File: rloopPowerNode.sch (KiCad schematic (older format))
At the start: 13 parts

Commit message: Switch to DPDT relay and rearranged stuff
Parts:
- removed K? (x2): RELAY, symbol RELAY
- removed Q?: Q_NJFET_DGS, symbol Q_NJFET_DGS
- removed U?: 74LS32, symbol 74LS32
- removed U?: Regulator, symbol Regulator
- removed U?: IsolatedRegulator, symbol IsolatedRegulator
- added C? (x2): C, symbol C
- added Q? (x2): Q_NMOS_GSD, symbol Q_NMOS_GSD
- added R? (x3): R, symbol R
- added RL?: Relay_DPDT, symbol Relay_DPDT
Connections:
- net labels added: DCDC_Vin+, DCDC_Vin-, LVEnablePin
- net labels removed: NodeControlPin
- wire segments 23 -> 33
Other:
- moved on the sheet: 10k, D?, R?, SW?

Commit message: work began
laid out some of the top level

started some lower level sub-circuits, such as relay drivers
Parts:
- removed 10k, R? (x5): R, symbol R
- removed C? (x2): C, symbol C
- removed D?: D, symbol D
- removed D?: LED, symbol LED
- removed Q? (x2): Q_NMOS_GSD, symbol Q_NMOS_GSD
- removed RL?: Relay_DPDT, symbol Relay_DPDT
- removed SW?: Switch_3PST, symbol Switch_3PST
- removed U?: 4541, symbol 4541
- added A?: Teensy_3.2, symbol Teensy_3.2
- added A?: RASPI_2B, symbol RASPI_2B
- added P?: CONN_01X09, symbol CONN_01X09
- added R? (x2): R, symbol R
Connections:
- net labels added: GLV, GNDA, HV-CURR, OSBMS-CLK, OSBMS-CS, OSBMS-IRQ, OSBMS-MISO, OSBMS-MOSI, OSBMS-PDLOWOUT, OSBMS-SCK, Pi-SCL, Pi-SDA, RLY-24V-HIGH, RLY-24V-LOW, RLY-ISO-HIGH, RLY-ISO-LOW, SENS-SCL, SENS-SDA
- net labels removed: +5V, +BATT, -BATT, DCDC_Vin+, DCDC_Vin-, LVEnablePin
- wire segments 33 -> 87
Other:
- note added: "To ATA6870\nOpen Source BMS"

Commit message: added some ICs, started on power, changed sheet sizes
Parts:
- added C? (x5): 100n, symbol C
- added P? (x4): CONN_01X02, symbol CONN_01X02
- added P?: CONN_01X04, Pin_Headers:Pin_Header_Straight_1x04_Pitch2.00mm, symbol CONN_01X04
- added U?: MCP2562, symbol MCP2562
- added U?: TYS01, symbol TYS01
- added U?: ISO1540, symbol ISO1540
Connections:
- net labels added: +3.3V, CAN-RX, CAN-TX
- wire segments 87 -> 162
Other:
- note added: "To baro sensor"

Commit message: near done, TODO needs 5V sup from HV, etc
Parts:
- removed A?: Teensy_3.2, symbol Teensy_3.2
- removed A?: RASPI_2B, symbol RASPI_2B
- removed C? (x4): 100n, symbol C
- removed P?: CONN_01X04, Pin_Headers:Pin_Header_Straight_1x04_Pitch2.00mm, symbol CONN_01X04
- removed R? (x2): R, symbol R
- removed U?: MCP2562, symbol MCP2562
- removed U?: TYS01, symbol TYS01
- removed U?: ISO1540, symbol ISO1540
- added A?: NODE_CORE_CONNECTOR, symbol NODE_CORE_CONNECTOR
- added C? (x3): 100n, symbol C
- added C? (x2): 1u, symbol C
- added D?: ZENER +2V8, symbol ZENER
- added P? (x4): CONN_01X03, Pin_Headers:Pin_Header_Angled_1x03, symbol CONN_01X03
- added P?: SHUNT, symbol CONN_01X02
- added Q?: BSS84, TO_SOT_Packages_SMD:SOT-23, symbol Q_PMOS_GSD
- added R?: 1M, Resistors_SMD:R_1206_HandSoldering, symbol R
- added R?: 100K, symbol R
- added R?: R, symbol R
- added U?: MS5607-02BA03, symbol MS5607-02BA03
- added U?: DS2482-100, symbol DS2482-100
- added U?: AMC1100, symbol AMC1100
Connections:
- net labels added: +5V-HV, HV-GND
- net labels removed: CAN-RX, CAN-TX, Pi-SCL, Pi-SDA
- wire segments 162 -> 149
- no-connect marks 0 -> 2
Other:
- note added: "4x strands, 10x sensors each"
- note added: "To ATA6870\nOpen Source BMS\nMultiple BMS will be daisy chained"
- note added: "barometric pressure sensor\nfor detecting depressurization"
- note added: "checks the GLV (+24V)"
- note added: "one temperature sensor for each cell"
- note added: "reads current from the HV battery\nlow side current shunt\nwhich is galvanically isolated"
- note removed: "To ATA6870\nOpen Source BMS"
- note removed: "To baro sensor"
- moved on the sheet: C?, P?

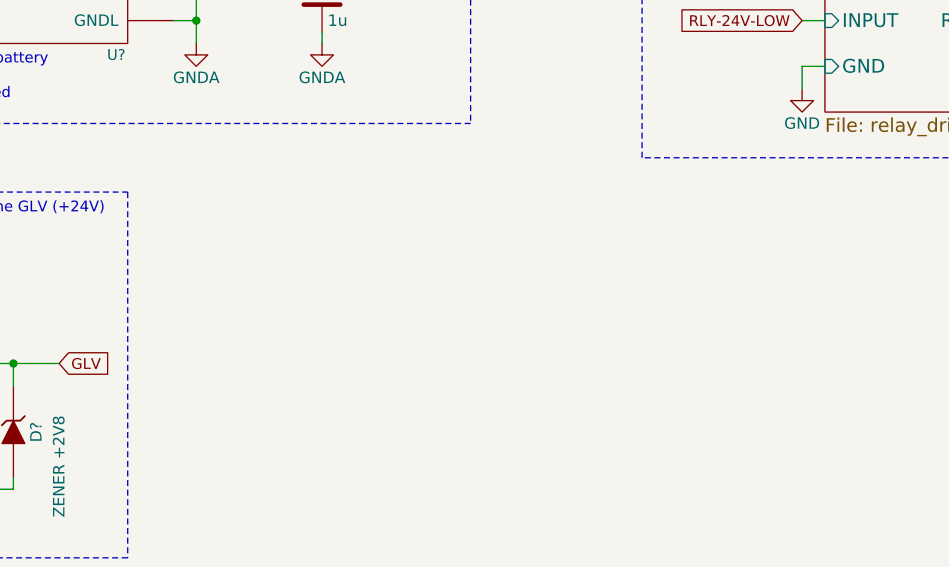
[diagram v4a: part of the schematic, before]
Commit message: added a 78L05 for the AMC1100
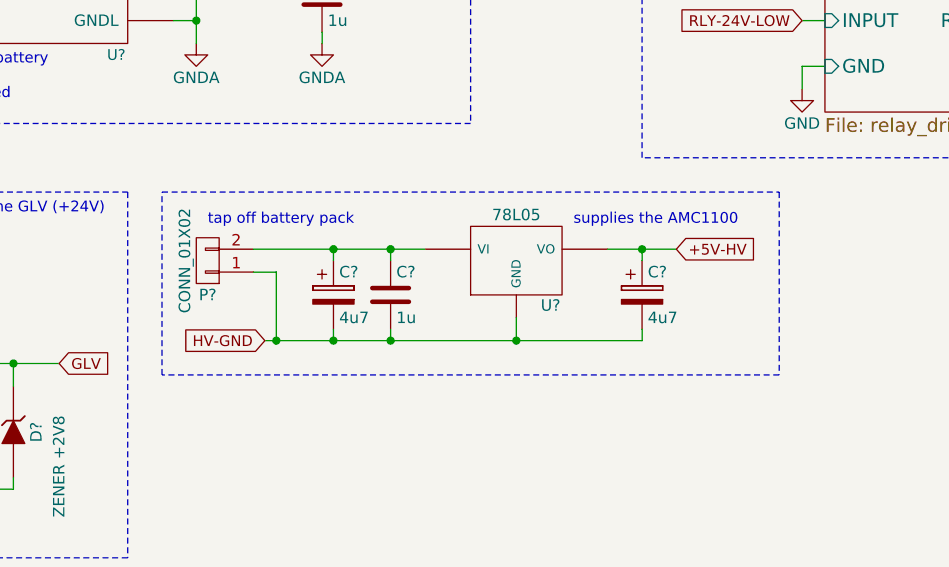
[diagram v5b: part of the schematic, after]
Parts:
- added C? (x2): 4u7, symbol CP
- added C?: 1u, symbol C
- added P?: CONN_01X02, symbol CONN_01X02
- added U?: 78L05, symbol 78L05
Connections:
- net Relay Driver/RELAY-NEG is gone; now on net Relay Driver/RELAY-NEG: P?.2 (P2)
- net Relay Driver/RELAY-POS is gone; now on net Relay Driver/RELAY-POS: P?.1 (P1)
- net +5V-HV: now also C?.1, U?.VO
- net HV-GND: now also C?.2, C?.2, C?.2, P?.1 (P1), U?.GND
- net Relay Driver/RELAY-NEG: no longer P?.2 (P2)
- net Relay Driver/RELAY-POS: no longer P?.1 (P1)
- new net: C?.1, C?.1, P?.2 (P2), U?.VI
- new net Relay Driver/RELAY-NEG: P?.2 (P2)
- new net Relay Driver/RELAY-POS: P?.1 (P1)
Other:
- note added: "supplies the AMC1100"
- note added: "tap off battery pack"
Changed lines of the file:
@@
 Wire Notes Line
 	8500 5250 8500 650
+$Comp
+L 78L05 U?
+U 1 1 573D5D57
+P 7950 5700
+F 0 "U?" H 8100 5504 50  0000 C CNN
+F 1 "78L05" H 7950 5900 50  0000 C CNN
+F 2 "" H 7950 5700 50  0000 C CNN
+F 3 "" H 7950 5700 50  0000 C CNN
+	1    7950 5700
+	1    0    0    -1
+$EndComp
+Text GLabel 6850 6050 0    47   Input ~ 0
+HV-GND
+$Comp
+L CONN_01X02 P?
+U 1 1 573D68FA
+P 6600 5700
+F 0 "P?" H 6600 5850 50  0000 C CNN
+F 1 "CONN_01X02" V 6700 5700 50  0000 C CNN
+F 2 "" H 6600 5700 50  0000 C CNN
+F 3 "" H 6600 5700 50  0000 C CNN
+	1    6600 5700
+	-1   0    0    1
+$EndComp
+$Comp
+L CP C?
+U 1 1 573D6D0A
+P 7150 5850
+F 0 "C?" H 7175 5950 50  0000 L CNN
+F 1 "4u7" H 7175 5750 50  0000 L CNN
+F 2 "" H 7188 5700 50  0000 C CNN
+F 3 "" H 7150 5850 50  0000 C CNN
+	1    7150 5850
+	1    0    0    -1
+$EndComp
+$Comp
+L C C?
+U 1 1 573D757D
+P 7400 5850
+F 0 "C?" H 7425 5950 50  0000 L CNN
+F 1 "1u" H 7425 5750 50  0000 L CNN
+F 2 "" H 7438 5700 50  0000 C CNN
+F 3 "" H 7400 5850 50  0000 C CNN
+	1    7400 5850
+	1    0    0    -1
+$EndComp
+$Comp
+L CP C?
+U 1 1 573D7783
+P 8500 5850
+F 0 "C?" H 8525 5950 50  0000 L CNN
+F 1 "4u7" H 8525 5750 50  0000 L CNN
+F 2 "" H 8538 5700 50  0000 C CNN
+F 3 "" H 8500 5850 50  0000 C CNN
+	1    8500 5850
+	1    0    0    -1
+$EndComp
+Wire Wire Line
+	6800 5750 6900 5750
+Wire Wire Line
+	6900 5750 6900 6050
+Wire Wire Line
+	6850 6050 8500 6050
+Wire Wire Line
+	8500 6050 8500 6000
+Connection ~ 6900 6050
+Wire Wire Line
+	7400 6000 7400 6050
+Connection ~ 7400 6050
+Wire Wire Line
+	7150 6000 7150 6050
+Connection ~ 7150 6050
+Wire Wire Line
+	7950 5950 7950 6050
+Connection ~ 7950 6050
+Wire Wire Line
+	8350 5650 8650 5650
+Wire Wire Line
+	8500 5700 8500 5650
+Connection ~ 8500 5650
+Wire Wire Line
+	7550 5650 6800 5650
+Wire Wire Line
+	7150 5700 7150 5650
+Connection ~ 7150 5650
+Wire Wire Line
+	7400 5700 7400 5650
+Connection ~ 7400 5650
+Text GLabel 8650 5650 2    47   Input ~ 0
++5V-HV
+Text Notes 8200 5550 0    47   ~ 0
+supplies the AMC1100
+Wire Notes Line
+	6400 5400 9100 5400
+Wire Notes Line
+	9100 5400 9100 6200
+Wire Notes Line
+	9100 6200 6400 6200
+Wire Notes Line
+	6400 6200 6400 5400
+Text Notes 6600 5550 0    47   ~ 0
+tap off battery pack
 $EndSCHEMATC

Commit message: wip showing you the latching power btn
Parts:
- added JP? (x8): Jumper_NC_Small, symbol Jumper_NC_Small
- added P? (x4): CONN_01X02, symbol CONN_01X02
- added P?: CONN_02X05, symbol CONN_02X05
- added R? (x3): R, symbol R
- added RL? (x3): Relay_DPDT, symbol Relay_DPDT
- added SW?: Switch_3PST, symbol Switch_3PST
- added U? (x2): LTV-358T, MFSOP-6, symbol LTV-358T
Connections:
- net GND: now also JP?.1, JP?.1, JP?.1, JP?.1, JP?.1, JP?.1, JP?.1, JP?.1, P?.10 (P10), P?.2 (P2), P?.4 (P4), P?.6 (P6), P?.8 (P8), U?.3
- net OSBMS-CS: now also P?.7 (P7)
- net OSBMS-MISO: now also P?.1 (P1)
- net OSBMS-MOSI: now also P?.3 (P3)
- net OSBMS-SCK: now also P?.5 (P5)
- net Relay Driver/RELAY-NEG: now also RL?.2; no longer P?.2 (P2)
- net Relay Driver/RELAY-POS: now also RL?.1; no longer P?.1 (P1)
- new net: P?.1 (P1), RL?.4, SW?.1
- new net: RL?.5, SW?.2
- new net: P?.2 (P2), RL?.7, SW?.3
- new net: RL?.8, SW?.4
- new net: P?.1 (P1), RL?.8
- new net: P?.2 (P2), R?.2, RL?.5
- new net: A?.~ (T9/RX2), JP?.2 (x8)
- new net: R?.2, RL?.1 (x2)
- new net: RL?.2, U?.6 (x2)
- new net: P?.2 (P2), R?.1, R?.1, R?.1, RL?.4, RL?.4
- new net: P?.1 (P1), RL?.7, U?.4, U?.4
- new net Relay Driver/RELAY-NEG: P?.2 (P2)
- new net Relay Driver/RELAY-POS: P?.1 (P1)
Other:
- note added: "one temperature sensor for every 2 cells"
- note removed: "one temperature sensor for each cell"
- moved on the sheet: A?, C?, D?, P?, Q?, R?, U?

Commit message: WIP but mostly done, needs connector
latch switch changed to using photorelays
added watchdog to relays
added two unidirectional precharge subcircuits
moved ILV relay to onboard
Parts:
- removed P? (x6): CONN_01X02, symbol CONN_01X02
- removed R? (x3): R, symbol R
- removed RL? (x3): Relay_DPDT, symbol Relay_DPDT
- removed SW?: Switch_3PST, symbol Switch_3PST
- removed U? (x2): LTV-358T, MFSOP-6, symbol LTV-358T
- added C?: 100n, symbol C
- added D? (x3): D, symbol D
- added JP?: JUMPER, symbol JUMPER
- added P?: CONN_01X02, symbol CONN_01X02
- added Q?: NMOS, symbol Q_NMOS_GDSD
- added Q? (x2): PMOS, symbol Q_PMOS_GDSD
- added R? (x4): 470, symbol R
- added R? (x3): 100K, symbol R
- added R?: 10K, symbol R
- added R?: 100, symbol R
- added R?: 1K, symbol R
- added R?: 10, symbol R
- added RL? (x2): Relay_DPDT, symbol Relay_DPDT
- added U? (x4): CPC1718, symbol CPC1718
- added U?: MAX6814, symbol WDT-5PIN-ACTIVELOW
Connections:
- net HV-GND is gone; now on net BATT-NEG: C?.1, C?.2, C?.2, C?.2, P?.1 (P1), P?.1 (P1), U?.3 (VinN), U?.4 (GNDH), U?.GND
- net RLY-24V-HIGH is gone; now on net SENS-SDA: A?.~ (T9/RX2)
- net RLY-24V-LOW is gone; now on net SENS-SDA: A?.~ (T9/RX2)
- net +3V3: now also C?.1, U?.5 (VDD)
- net BATT-NEG: now also RL?.7, U?.2, U?.2, U?.2
- net BATT-POS: now also Q?.3 (S), R?.1, RL?.4, U?.1
- net GND: now also C?.2, Q?.3 (S), R?.2, U?.2 (GND), U?.3, U?.3
- net Relay Driver/RELAY-NEG: now also RL?.2; no longer P?.2 (P2)
- net Relay Driver/RELAY-POS: now also RL?.1; no longer P?.1 (P1)
- net BMS-PWR: now reaches P?.9 (P9)
- net ILV+: now reaches C?.1, C?.1, P?.2 (P2), U?.VI
- net ILV+: now also RL?.5
- new net: R?.1, U?.3
- new net: D?.1 (K), U?.4
- new net: P?.1 (P1), U?.3
- new net: R?.2, U?.4
- new net: D?.2 (A), P?.2 (P2)
- new net: Q?.1 (G), R?.1
- new net: JP?.2, Q?.2 (D), Q?.4 (D)
- new net: R?.1, R?.2, U?.1 (~OUTPUT)
- new net: Q?.1 (G), R?.1, R?.2 (x2)
- new net: D?.2 (A), Q?.2 (D), Q?.4 (D) (x2)
- new net: R?.2, U?.1 (x2)
- new net: R?.1, U?.4 (x2)
- new net: D?.1 (K), R?.1 (x2)
- new net BATT-ILV: Q?.3 (S), R?.1, RL?.4
- new net DCDC-NEG: RL?.8, U?.1
- new net DCDC-POS: RL?.5, U?.2
- new net IHV-EXTERNAL: R?.2
- new net IHV-PRECHG: R?.2
- new net ILV-EXTERNAL: R?.2
- new net ILV-PRECHG: R?.2
- new net RELAY-COMMON: JP?.1
- new net RLY-ILV: A?.~ (T9/RX2)
- new net Relay Driver/RELAY-NEG: P?.2 (P2)
- new net Relay Driver/RELAY-NEG: RL?.2
- new net Relay Driver/RELAY-POS: P?.1 (P1)
- new net Relay Driver/RELAY-POS: RL?.1
- new net WDT: U?.4 (INPUT)
- no-connect marks 2 -> 3
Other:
- note added: "Precharge IHV"
- note added: "Precharge ILV"
- note added: "TODO: Give connectors to external stuff\nTODO: Pin assignments for unassigned signals\nTODO: Review suggested change to BMS connector\n"
- note added: "Use external battery as "ignition""
- note added: "Watchdog to kill all power"
- note added: "manual disconnect"
- note added: "suggested connector to Open Source BMS\nribbon cable with grounds add noise immunity"
- note removed: "tap off battery pack"
- moved on the sheet: A?, C?, D?, JP?, P?, Q?, R?, U?

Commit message: added GND fault detect, conns, no pending TODOs
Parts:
- removed D?: D, symbol D
- removed JP?: JUMPER, symbol JUMPER
- removed P?: CONN_01X09, symbol CONN_01X09
- removed Q? (x2): PMOS, symbol Q_PMOS_GDSD
- removed R? (x2): 470, symbol R
- removed R?: 10K, symbol R
- removed R? (x2): 100K, symbol R
- removed R?: 100, symbol R
- removed R?: 1K, symbol R
- removed R?: 10, symbol R
- removed RL?: Relay_DPDT, symbol Relay_DPDT
- removed U?: CPC1718, symbol CPC1718
- added D? (x2): D, symbol D
- added D?: ZENER +3V6, symbol ZENER
- added D?: LED, symbol Led_Small
- added F? (x2): FUSE, symbol FUSE
- added JP?: JUMPER3, symbol JUMPER3
- added P? (x7): CONN_01X02, symbol CONN_01X02
- added P? (x6): CONN_01X01, symbol CONN_01X01
- added P?: CONN_01X08, symbol CONN_01X08
- added Q?: PMOS, symbol Q_PMOS_GSD
- added Q?: NMOS, symbol Q_NMOS_GDSD
- added R? (x2): 100, symbol R
- added R?: 470, symbol R
- added R?: 100K, symbol R
- added R?: 10K, symbol R
- added R?: 1K8, symbol R
- added R?: 330, symbol R
- added R?: 10, symbol R
- added U?: CPC1718, symbol CPC1718
- added U?: H11F1SM, MFSOP-6, symbol OPTOISO
- C?: value 1u -> 100n
- D?: value ZENER +2V8 -> ZENER +2V7
- P?: value CONN_02X05 -> AMPMODU-02X05
- R?: value 1M -> 100K
- R?: value 100K -> 10K
- R?: value R -> 100
- R?: value 470 -> 100
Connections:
- net +24V: now also P?.2 (P2), P?.2 (P2)
- net +3V3: no longer C?.1, U?.5 (VDD)
- net BATT-ILV: now also P?.1 (P1), R?.2
- net BATT-NEG: now also P?.1 (P1); no longer C?.1, C?.2, C?.2, C?.2, P?.1 (P1), P?.1 (P1), U?.2, U?.3 (VinN), U?.4 (GNDH), U?.GND
- net BATT-POS: now also P?.2 (P2), R?.2
- net DCDC-NEG: now also C?.1, C?.2, C?.2, C?.2, P?.1 (P1), P?.1 (P1), U?.3 (VinN), U?.4 (GNDH), U?.GND, P?.1 (P1), P?.1 (P1), P?.1 (P1), P?.2 (P2)
- net DCDC-POS: now also F?.1, P?.1 (P1), P?.2 (P2), P?.2 (P2)
- net GND: now also D?.2 (A), JP?.3, P?.1 (P1), P?.1 (P1), P?.1 (P1), R?.1, R?.1, U?.3, U?.4
- net IHV-EXTERNAL: now also D?.1 (K), P?.1 (P1)
- net IHV-PRECHG: now also A?.~ (T9/RX2)
- net ILV-EXTERNAL: now also D?.1 (K), P?.1 (P1)
- net ILV-PRECHG: now also A?.~ (T9/RX2), R?.2
- net RELAY-COMMON: now also JP?.2
- net RLY-DCDC: now also A?.~ (T9/RX2)
- net Relay Driver/RELAY-NEG: now also P?.2 (P2); no longer P?.2 (P2)
- net Relay Driver/RELAY-POS: now also P?.1 (P1); no longer P?.1 (P1)
- net WDT: now also A?.~ (T9/RX2)
- net ~GNDFAULT: now reaches A?.~ (T9/RX2)
- net ~GNDFAULT: now also D?.1 (K), Q?.1 (G), R?.2, R?.2
- net at U?.3: now also U?.4
- net at U?.3: now also U?.1; no longer P?.1 (P1)
- net at Q?.2 (D), Q?.4 (D): now also Q?.3 (S)
- net at D?.2 (A): now also U?.2
- net at U?.1: now also R?.1
- new net: D?.1 (K), P?.1 (P1)
- new net: C?.1, Q?.3 (D), R?.2, U?.5 (VDD)
- new net: R?.1, U?.1
- new net: D?.2 (A), U?.2 (x2)
- new net: R?.1, U?.4
- new net: Q?.1 (G), R?.1
- new net: JP?.1, Q?.2 (D), Q?.4 (D), R?.2, R?.2, U?.6
- new net: D?.1 (K), D?.2 (A)
- new net: F?.2, P?.2 (P2)
- new net: P?.1 (P1), P?.3 (P3)
- new net: P?.1 (P1), P?.4 (P4)
- new net: P?.8 (P8), R?.1
- new net: F?.1, F?.2
- new net +5V: A?.~ (T9/RX2), Q?.2 (S), R?.1
- new net Relay Driver/RELAY-NEG: P?.2 (P2)
- new net Relay Driver/RELAY-POS: P?.1 (P1)
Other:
- note added: "22V divided to something\nthe Teensy can read\nbut total pull-down of 2K"
- note added: "Operate optoisolator LEDs at 30mA\nPerhaps a current limiter instead of resistor"
- note added: "Watchdog to kill all power\nThe pulse will kill the NMOS\nwhich subsequently kills the PMOS\nas long as the optocoupler is off"
- note added: "chassis"
- note added: "connect to ISOMETER HV"
- note added: "connect to Open Source BMS"
- note added: "connector to\nISOMETER IR155-3203"
- note added: "ground fault event\nwill kill all relays"
- note added: "manual disconnect\n1A capable\nsuggest adding a \nplastic pull ring\nto the jumper"
- note added: "off-leakage = 1uA"
- note added: "output gain is 8x\noptional PGA inside Teensy\nup to 64x"
- note added: "to DCDC converter module\noptional fuse\noptional inrush limiter"
- note added: "to ground fault detector"
- note removed: "4x strands, 10x sensors each"
- note removed: "Precharge IHV"
- note removed: "Precharge ILV"
- note removed: "TODO: Give connectors to external stuff\nTODO: Pin assignments for unassigned signals\nTODO: Review suggested change to BMS connector\n"
- note removed: "To ATA6870\nOpen Source BMS\nMultiple BMS will be daisy chained"
- note removed: "Watchdog to kill all power"
- note removed: "manual disconnect"
- note removed: "suggested connector to Open Source BMS\nribbon cable with grounds add noise immunity"
- moved on the sheet: C?, D?, P?, Q?, R?, RL?, U?
